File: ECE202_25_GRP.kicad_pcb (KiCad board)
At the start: 2 copper layers, 0 parts

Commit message: Schematic Repairs, v1 PCB
Replaced bus with wires in schematic, added footprints to resistors, caps, pins in schematic.

Imported schematic into PCB, designed PCB.
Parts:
- added C1: 100uF, Capacitor_SMD:C_1206_3216Metric, F.Cu at (132.6, 101.6)
- added J1: Run_in+, Connector_PinHeader_2.54mm:PinHeader_1x01_P2.54mm_Vertical, F.Cu at (133.1, 69.1)
- added J2: Brake_in+, Connector_PinHeader_2.54mm:PinHeader_1x01_P2.54mm_Vertical, F.Cu at (117.9, 69.1)
- added J3: Turn_in+, Connector_PinHeader_2.54mm:PinHeader_1x01_P2.54mm_Vertical, F.Cu at (125.5, 69.1)
- added J4: Run_out+, Connector_PinHeader_2.54mm:PinHeader_1x01_P2.54mm_Vertical, F.Cu at (166.1, 69.1)
- added J5: Brake_out+, Connector_PinHeader_2.54mm:PinHeader_1x01_P2.54mm_Vertical, F.Cu at (150.9, 69.1)
- added J6: Turn_out+, Connector_PinHeader_2.54mm:PinHeader_1x01_P2.54mm_Vertical, F.Cu at (158.5, 69.1)
- added J7: 9v_in, Connector_PinHeader_1.00mm:PinHeader_1x01_P1.00mm_Vertical, F.Cu at (116.8, 95.2)
- added J8: Ground, Connector_PinHeader_1.00mm:PinHeader_1x01_P1.00mm_Vertical, F.Cu at (116.8, 101.1)
- added K1: Running_Relay, Relay_THT:Relay_SPDT_Hongfa_JQC-3FF_0XX-1Z, F.Cu at (155.4, 89.0)
- added K2: Turn_Relay, Relay_THT:Relay_SPDT_Hongfa_JQC-3FF_0XX-1Z, F.Cu at (136.1, 89.0)
- added K3: Brake_Relay, Relay_THT:Relay_SPDT_Hongfa_JQC-3FF_0XX-1Z, F.Cu at (117.1, 89.0)
- added R1: 4700, Resistor_SMD:R_2010_5025Metric, F.Cu at (138.4, 98.5)
- added R2: 4700, Resistor_SMD:R_2010_5025Metric, F.Cu at (133.1, 96.8)
- added R3: 430, Resistor_SMD:R_0805_2012Metric, F.Cu at (143.1, 95.0)
- added R4: 430, Resistor_SMD:R_0805_2012Metric, F.Cu at (123.8, 94.5)
- added R5: 430, Resistor_SMD:R_0805_2012Metric, F.Cu at (160.4, 94.5)
- added U1: NE555P, Package_DIP:DIP-8_W7.62mm, F.Cu at (148.3, 102.6)
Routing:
- net GND: track 0.00 -> 124.7 mm
- net +9V: track 0.00 -> 84.9 mm
- net Net-(U1-THR): track 0.00 -> 57.0 mm
- net Net-(J1-Pin_1): track 0.00 -> 34.5 mm
- net Net-(J5-Pin_1): track 0.00 -> 29.8 mm
- net Net-(J3-Pin_1): track 0.00 -> 24.4 mm
- net Net-(J2-Pin_1): track 0.00 -> 20.9 mm
- net Net-(U1-DIS): track 0.00 -> 18.8 mm
- net Net-(J6-Pin_1): track 0.00 -> 13.6 mm
- net Net-(U1-Q): track 0.00 -> 12.6 mm
- net Net-(J4-Pin_1): track 0.00 -> 8.30 mm
- net Net-(K2-Pad11): track 0.00 -> 3.98 mm
- net Net-(K3-Pad11): track 0.00 -> 3.52 mm
- net Net-(K1-Pad11): track 0.00 -> 3.50 mm
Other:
- board outline added: 57.9 x 39.6 mm
- board text added: "HME Designs Tail Light Mainboard"

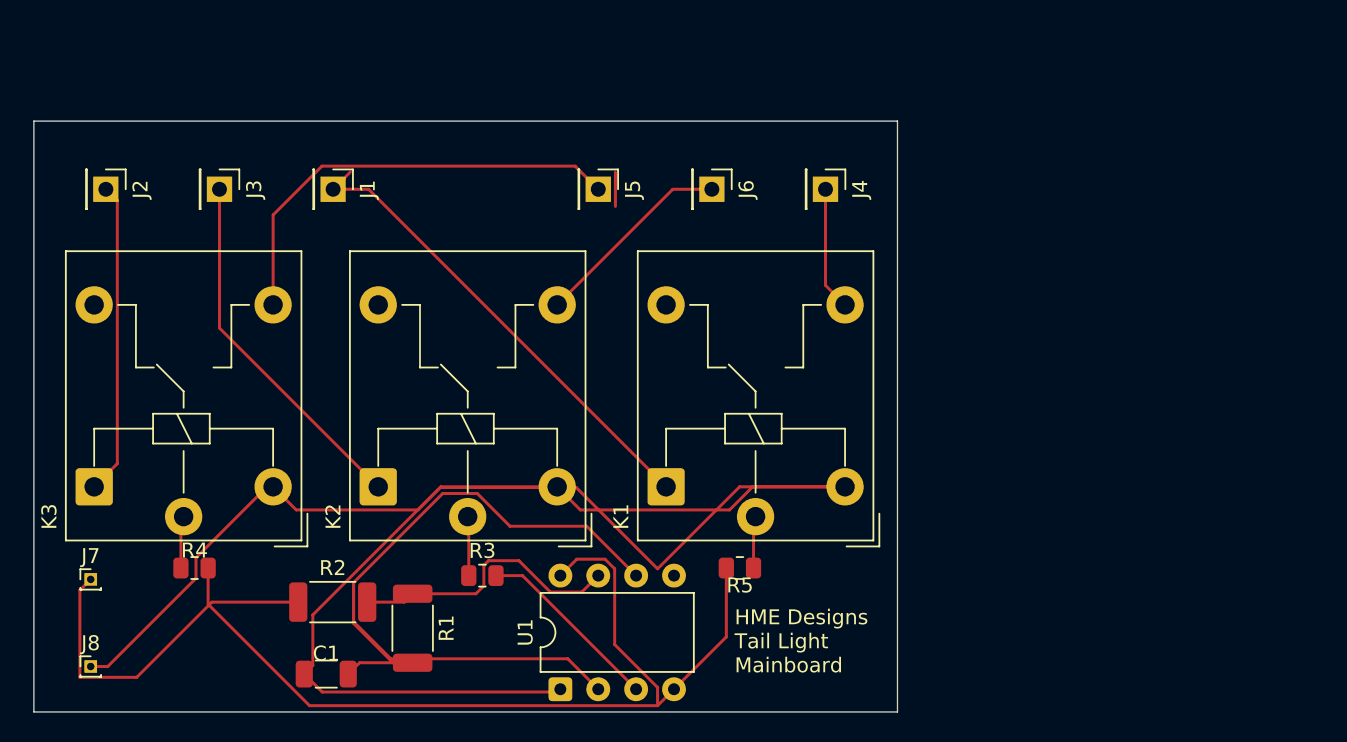
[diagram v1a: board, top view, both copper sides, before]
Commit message: PCB Production
Production files generated, order screenshot added to images folder. PCB order started today 3-18-25
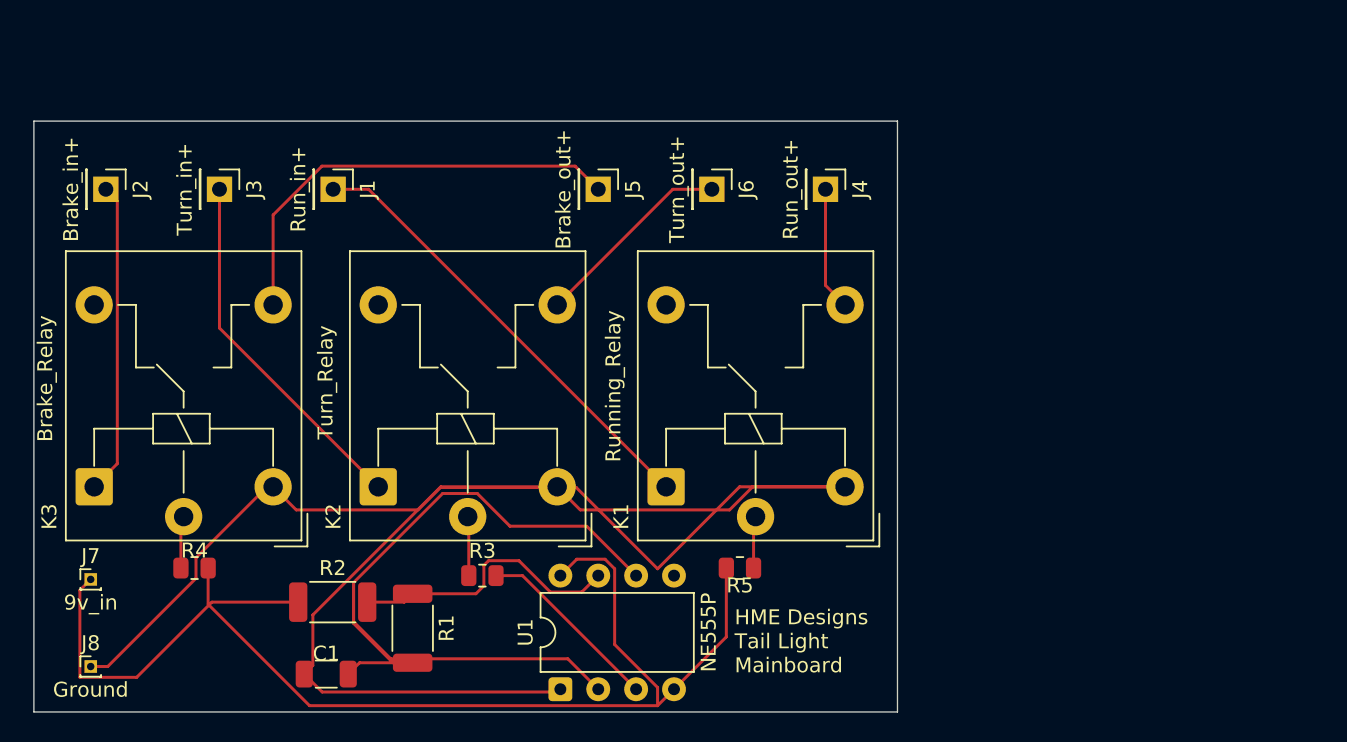
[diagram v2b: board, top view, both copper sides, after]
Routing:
- net Net-(J1-Pin_1): track 34.5 -> 30.6 mm
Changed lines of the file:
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@@
 		(property "Value" "Brake_Relay"
 			(at 7.2525 -3.2805 90)
-			(layer "F.Fab")
+			(layer "F.SilkS")
 			(effects
 				(font
@@
 		(property "Value" "Turn_Relay"
 			(at 7 -3.5345 90)
-			(layer "F.Fab")
+			(layer "F.SilkS")
 			(effects
 				(font
@@
 		(property "Value" "NE555P"
 			(at 3.81 9.95 90)
-			(layer "F.Fab")
+			(layer "F.SilkS")
 			(effects
 				(font
@@
 		(property "Value" "Turn_in+"
 			(at 0 2.33 90)
-			(layer "F.Fab")
+			(layer "F.SilkS")
 			(effects
 				(font
@@
 		(property "Value" "Brake_out+"
 			(at 0 2.33 90)
-			(layer "F.Fab")
+			(layer "F.SilkS")
 			(effects
 				(font
@@
 		(property "Value" "Ground"
 			(at 0 1.56 0)
-			(layer "F.Fab")
+			(layer "F.SilkS")
 			(effects
 				(font
@@
 		(property "Value" "Run_out+"
 			(at 0 2.33 90)
-			(layer "F.Fab")
+			(layer "F.SilkS")
 			(effects
 				(font
@@
 		(property "Value" "Running_Relay"
 			(at 6.7445 -3.5345 90)
-			(layer "F.Fab")
+			(layer "F.SilkS")
 			(effects
 				(font
@@
 		(property "Value" "9v_in"
 			(at 0 1.56 0)
-			(layer "F.Fab")
+			(layer "F.SilkS")
 			(effects
 				(font
@@
 		(property "Value" "Brake_in+"
 			(at 0 2.33 90)
-			(layer "F.Fab")
+			(layer "F.SilkS")
 			(effects
 				(font
@@
 		(property "Value" "Turn_out+"
 			(at 0 2.33 90)
-			(layer "F.Fab")
+			(layer "F.SilkS")
 			(effects
 				(font
@@
 		(property "Value" "Run_in+"
 			(at 0 2.33 90)
-			(layer "F.Fab")
+			(layer "F.SilkS")
 			(effects
 				(font
@@
 		(width 0.2)
 		(layer "F.Cu")
-		(net 3)
-	)
-	(segment
-		(start 152.027 67.937)
-		(end 152.027 70.239)
-		(width 0.2)
-		(layer "F.Cu")
-		(net 3)
-	)
-	(segment
-		(start 133.096 69.088)
-		(end 134.247 67.937)
-		(width 0.2)
-		(layer "F.Cu")

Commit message: V1 pcb updates, V2 pcb creation
Fixed a couple traces on V1 board, added missing ground pin. Changed pad sizes for SMD components to match on-hand inventory.

Created V2 project. Schematic done, PCB done. PCB ordered.
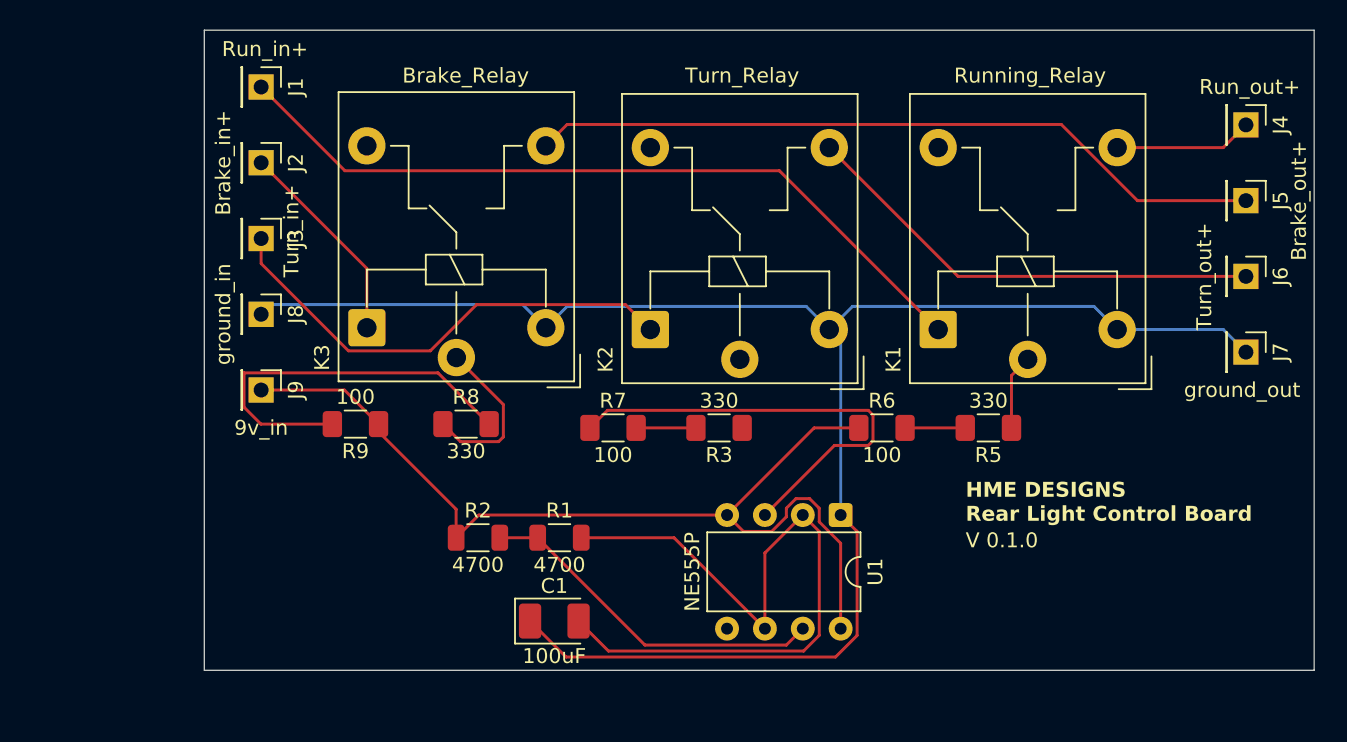
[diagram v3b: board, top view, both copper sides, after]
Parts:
- removed R4: 430, Resistor_SMD:R_0805_2012Metric
- added J9: 9v_in, Connector_PinHeader_2.54mm:PinHeader_1x01_P2.54mm_Vertical, F.Cu at (128.3, 82.5)
- added R6: 100, Resistor_SMD:R_1206_3216Metric_Pad1.30x1.75mm_HandSolder, F.Cu at (169.9, 85.1)
- added R7: 100, Resistor_SMD:R_1206_3216Metric_Pad1.30x1.75mm_HandSolder, F.Cu at (151.9, 85.1)
- added R8: 330, Resistor_SMD:R_1206_3216Metric_Pad1.30x1.75mm_HandSolder, F.Cu at (142.0, 84.8)
- added R9: 100, Resistor_SMD:R_1206_3216Metric_Pad1.30x1.75mm_HandSolder, F.Cu at (134.6, 84.8)
- C1: footprint Capacitor_SMD:C_1206_3216Metric -> Capacitor_Tantalum_SMD:CP_EIA-3528-12_Kemet-T_Pad1.50x2.35mm_HandSolder
- J7: value 9v_in -> ground_out; footprint Connector_PinHeader_1.00mm:PinHeader_1x01_P1.00mm_Vertical -> Connector_PinHeader_2.54mm:PinHeader_1x01_P2.54mm_Vertical
- J8: value Ground -> ground_in; footprint Connector_PinHeader_1.00mm:PinHeader_1x01_P1.00mm_Vertical -> Connector_PinHeader_2.54mm:PinHeader_1x01_P2.54mm_Vertical
- R1, R2: footprint Resistor_SMD:R_2010_5025Metric -> Resistor_SMD:R_1206_3216Metric
- R3, R5: value 430 -> 330; footprint Resistor_SMD:R_0805_2012Metric -> Resistor_SMD:R_1206_3216Metric_Pad1.30x1.75mm_HandSolder
- moved J7 79.0 mm to (194.3, 80.0), turned to -90 degrees
- moved J5 43.4 mm to (194.3, 69.8)
- moved J6 36.3 mm to (194.3, 74.9)
- moved J4 28.5 mm to (194.3, 64.8)
- moved J8 26.2 mm to (128.3, 77.5), turned to -90 degrees
- moved U1 22.1 mm to (167.1, 90.9), turned to -90 degrees
- moved K3 21.2 mm to (135.4, 78.4)
- moved K1 21.1 mm to (173.7, 78.5)
- moved K2 21.1 mm to (154.4, 78.5)
- moved R5 19.1 mm to (177.0, 85.1)
- moved R3 18.7 mm to (159.0, 85.1), turned to 180 degrees
- moved C1 15.7 mm to (147.9, 98.0)
- moved R1 11.6 mm to (148.3, 92.5), turned to 0 degrees
- moved R2 10.7 mm to (142.8, 92.5)
- moved J2 10.6 mm to (128.3, 67.3)
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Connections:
- J7 pad 1: +9V -> GND
- R3 pad 2: Net-(U1-Q) -> Net-(R3-Pad2)
- R5 pad 2: +9V -> Net-(R5-Pad2)
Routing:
- net Net-(R8-Pad2): track 0.00 -> 26.6 mm
- net Net-(J1-Pin_1): track 30.6 -> 52.1 mm
- net Net-(J5-Pin_1): track 29.8 -> 49.7 mm
- net +9V: track 84.9 -> 65.5 mm
- net Net-(U1-Q): track 12.6 -> 30.6 mm
- net Net-(J6-Pin_1): track 13.6 -> 31.5 mm
- net GND: track 124.7 -> 114.9 mm
- net Net-(J3-Pin_1): track 24.4 -> 32.2 mm
- net Net-(K3-Pad11): track 3.52 -> 11.3 mm
- net Net-(U1-THR): track 57.0 -> 49.4 mm
- net Net-(J2-Pin_1): track 20.9 -> 14.0 mm
- net Net-(U1-DIS): track 18.8 -> 23.8 mm
- net Net-(R5-Pad2): track 0.00 -> 4.04 mm
- net Net-(R3-Pad2): track 0.00 -> 4.01 mm
- net Net-(K2-Pad11): track 3.98 -> 0.00 mm
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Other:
- board size 57.9 x 39.6 mm -> 74.4 x 42.9 mm
- board text added: "HME DESIGNS Rear Light Control Board"
- board text added: "V 0.1.0"
- board text removed: "HME Designs Tail Light Mainboard"
